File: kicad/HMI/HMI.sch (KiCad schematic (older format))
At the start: 46 parts, among them J2 SWD, J3 DEM 128128A TMH-PW-N, J4 RIBBON, SW1 SW_Push, SW10 SW_Push, SW11 SW_Push, SW12 SW_Push, SW13 SW_Push, SW14 SW_Push, SW15 SW_Push, SW16 SW_Push, SW17 SW_Push, SW18 SW_Push, SW19 SW_Push, SW2 SW_Push, SW20 SW_Push, SW3 SW_Push, SW4 SW_Push, SW5 SW_Push, SW6 SW_Push, SW7 SW_Push, SW8 SW_Push, SW9 SW_Push, U1 STM32L011K4Tx, X1 ASV-4.000MHZ-EJ-T

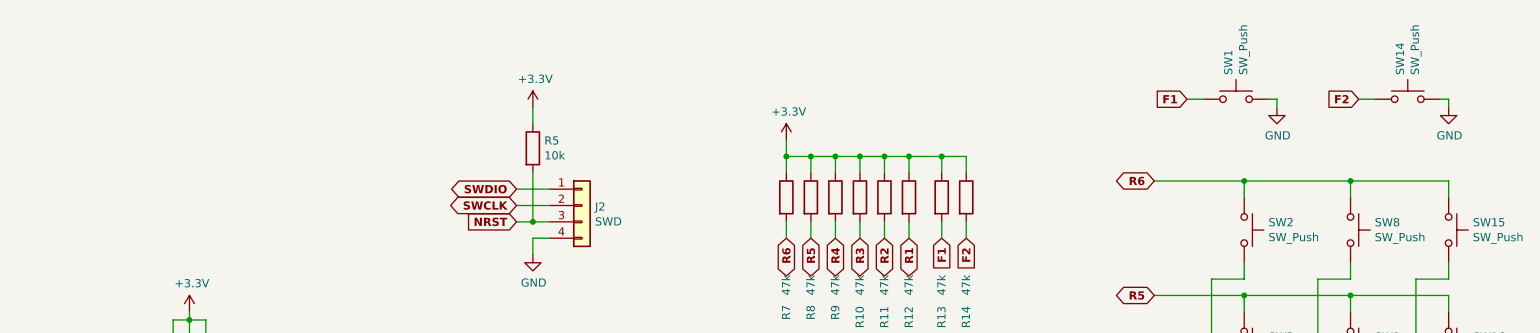
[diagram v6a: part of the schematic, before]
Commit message: HMI -> corrected PCB to mainboard form factor, added diodes
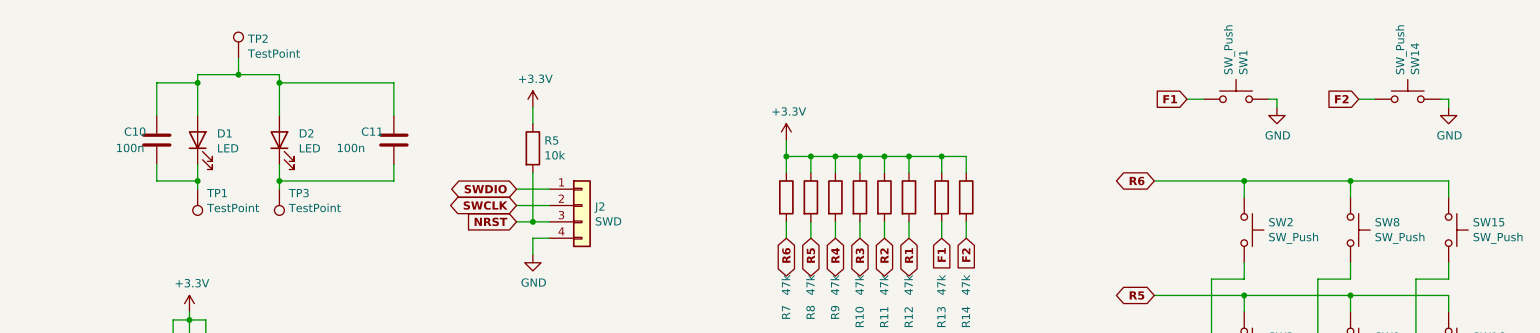
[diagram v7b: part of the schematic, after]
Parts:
- added C10, C11: 100n, Capacitor_SMD:C_0603_1608Metric, symbol Device:C
- added D1, D2: LED, Diode_SMD:D_0603_1608Metric, symbol Device:LED
- added TP1, TP2, TP3: TestPoint, TestPoint:TestPoint_Pad_2.0x2.0mm, symbol Connector:TestPoint
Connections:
- net F1: now also SW1.2; no longer SW1.1
- net F2: now also SW14.2; no longer SW14.1
- net GND: now also SW1.1, SW14.1; no longer SW1.2, SW14.2
- new net: C10.2, D1.1 (K), TP1.1
- new net: C10.1, C11.1, D1.2 (A), D2.2 (A), TP2.1
- new net: C11.2, D2.1 (K), TP3.1
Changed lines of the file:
@@
 F 3 "~" H 8650 1400 50  0001 C CNN
 	1    8650 1200
-	1    0    0    -1
+	-1   0    0    -1
 $EndComp
 $Comp
@@
 F 3 "~" H 9700 1400 50  0001 C CNN
 	1    9700 1200
-	1    0    0    -1
+	-1   0    0    -1
 $EndComp
 $Comp
@@
 	4300 3750 4300 3650
 Connection ~ 4200 3750
+$Comp
+L Device:LED D1
+U 1 1 5F2DC0D1
+P 2300 1450
+F 0 "D1" V 2339 1332 50  0000 R CNN
+F 1 "LED" V 2248 1332 50  0000 R CNN
+F 2 "Diode_SMD:D_0603_1608Metric" H 2300 1450 50  0001 C CNN
+F 3 "~" H 2300 1450 50  0001 C CNN
+	1    2300 1450
+	0    -1   -1   0
+$EndComp
+$Comp
+L Device:LED D2
+U 1 1 5F2E1112
+P 2800 1450
+F 0 "D2" V 2839 1332 50  0000 R CNN
+F 1 "LED" V 2748 1332 50  0000 R CNN
+F 2 "Diode_SMD:D_0603_1608Metric" H 2800 1450 50  0001 C CNN
+F 3 "~" H 2800 1450 50  0001 C CNN
+	1    2800 1450
+	0    -1   -1   0
+$EndComp
+Wire Wire Line
+	2800 1300 2800 1100
+Wire Wire Line
+	2800 1050 2550 1050
+Wire Wire Line
+	2300 1050 2300 1100
+$Comp
+L Connector:TestPoint TP2
+U 1 1 5F3017E8
+P 2550 950
+F 0 "TP2" H 2608 1068 50  0000 L CNN
+F 1 "TestPoint" H 2608 977 50  0000 L CNN
+F 2 "TestPoint:TestPoint_Pad_2.0x2.0mm" H 2750 950 50  0001 C CNN
+F 3 "~" H 2750 950 50  0001 C CNN
+	1    2550 950
+	1    0    0    -1
+$EndComp
+Wire Wire Line
+	2550 950  2550 1050
+Connection ~ 2550 1050
+Wire Wire Line
+	2550 1050 2300 1050
+$Comp
+L Connector:TestPoint TP3
+U 1 1 5F3133F8
+P 2800 1750
+F 0 "TP3" H 2742 1776 50  0000 R CNN
+F 1 "TestPoint" H 2742 1867 50  0000 R CNN
+F 2 "TestPoint:TestPoint_Pad_2.0x2.0mm" H 3000 1750 50  0001 C CNN
+F 3 "~" H 3000 1750 50  0001 C CNN
+	1    2800 1750
+	-1   0    0    1
+$EndComp
+$Comp
+L Connector:TestPoint TP1
+U 1 1 5F313DFF
+P 2300 1750
+F 0 "TP1" H 2242 1776 50  0000 R CNN
+F 1 "TestPoint" H 2242 1867 50  0000 R CNN
+F 2 "TestPoint:TestPoint_Pad_2.0x2.0mm" H 2500 1750 50  0001 C CNN
+F 3 "~" H 2500 1750 50  0001 C CNN
+	1    2300 1750
+	-1   0    0    1
+$EndComp
+Wire Wire Line
+	2800 1750 2800 1700
+Wire Wire Line
+	2300 1750 2300 1700
+$Comp
+L Device:C C10
+U 1 1 5F36D618
+P 2050 1450
+F 0 "C10" H 1850 1500 50  0000 L CNN
+F 1 "100n" H 1800 1400 50  0000 L CNN
+F 2 "Capacitor_SMD:C_0603_1608Metric" H 2088 1300 50  0001 C CNN
+F 3 "~" H 2050 1450 50  0001 C CNN
+	1    2050 1450
+	1    0    0    -1
+$EndComp
+$Comp
+L Device:C C11
+U 1 1 5F36ECB9
+P 3500 1450
+F 0 "C11" H 3300 1500 50  0000 L CNN
+F 1 "100n" H 3150 1400 50  0000 L CNN
+F 2 "Capacitor_SMD:C_0603_1608Metric" H 3538 1300 50  0001 C CNN
+F 3 "~" H 3500 1450 50  0001 C CNN
+	1    3500 1450
+	1    0    0    -1
+$EndComp
+Wire Wire Line
+	3500 1300 3500 1100
+Wire Wire Line
+	3500 1100 2800 1100
+Connection ~ 2800 1100
+Wire Wire Line
+	2800 1100 2800 1050
+Wire Wire Line
+	3500 1600 3500 1700
+Wire Wire Line
+	3500 1700 2800 1700
+Connection ~ 2800 1700
+Wire Wire Line
+	2800 1700 2800 1600
+Wire Wire Line
+	2050 1600 2050 1700
+Wire Wire Line
+	2050 1700 2300 1700
+Connection ~ 2300 1700
+Wire Wire Line
+	2300 1700 2300 1600
+Wire Wire Line
+	2050 1100 2300 1100
+Wire Wire Line
+	2050 1100 2050 1300
+Connection ~ 2300 1100
+Wire Wire Line
+	2300 1100 2300 1300
 $EndSCHEMATC

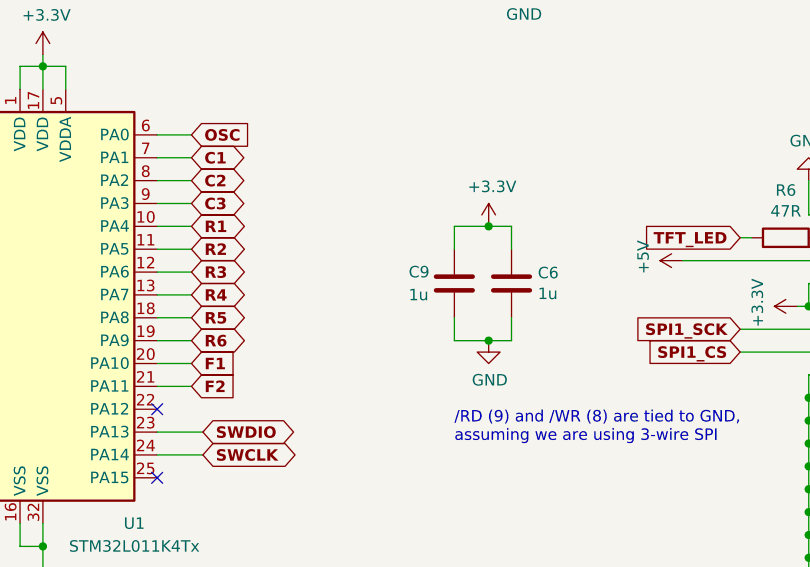
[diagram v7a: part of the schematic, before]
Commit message: HMI: added labels on silksScreen -> added one capacitor -> generated new PDF -> generated new GERBERS -> NEW STEP!
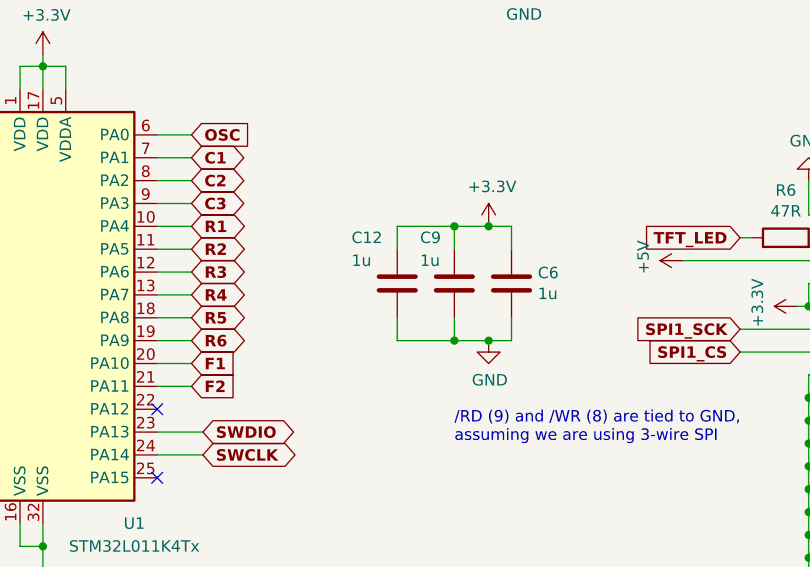
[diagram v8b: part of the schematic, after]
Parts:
- added C12: 1u, Capacitor_SMD:C_0603_1608Metric, symbol Device:C
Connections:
- net +3V3: now also C12.1
- net GND: now also C12.2
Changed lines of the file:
@@
 U 1 1 5F2AFB96
 P 4050 3500
-F 0 "C9" H 3850 3550 50  0000 L CNN
-F 1 "1u" H 3850 3450 50  0000 L CNN
+F 0 "C9" H 3900 3700 50  0000 L CNN
+F 1 "1u" H 3900 3600 50  0000 L CNN
 F 2 "Capacitor_SMD:C_0603_1608Metric" H 4088 3350 50  0001 C CNN
 F 3 "~" H 4050 3500 50  0001 C CNN
@@
 Wire Wire Line
 	2300 1100 2300 1300
+$Comp
+L Device:C C12
+U 1 1 5F2849DE
+P 3800 3500
+F 0 "C12" H 3600 3700 50  0000 L CNN
+F 1 "1u" H 3600 3600 50  0000 L CNN
+F 2 "Capacitor_SMD:C_0603_1608Metric" H 3838 3350 50  0001 C CNN
+F 3 "~" H 3800 3500 50  0001 C CNN
+	1    3800 3500
+	1    0    0    -1
+$EndComp
+Wire Wire Line
+	4050 3250 3800 3250
+Wire Wire Line
+	3800 3250 3800 3350
+Connection ~ 4050 3250
+Wire Wire Line
+	3800 3650 3800 3750
+Wire Wire Line
+	3800 3750 4050 3750
+Connection ~ 4050 3750
 $EndSCHEMATC
